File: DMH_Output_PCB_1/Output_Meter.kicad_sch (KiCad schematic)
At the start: 63 parts, among them Q1 BC558, Q2 BC558, U1 TL072, U2 LM339, U3 LM339, U4 LM339, U5 LM339, U6 LM339

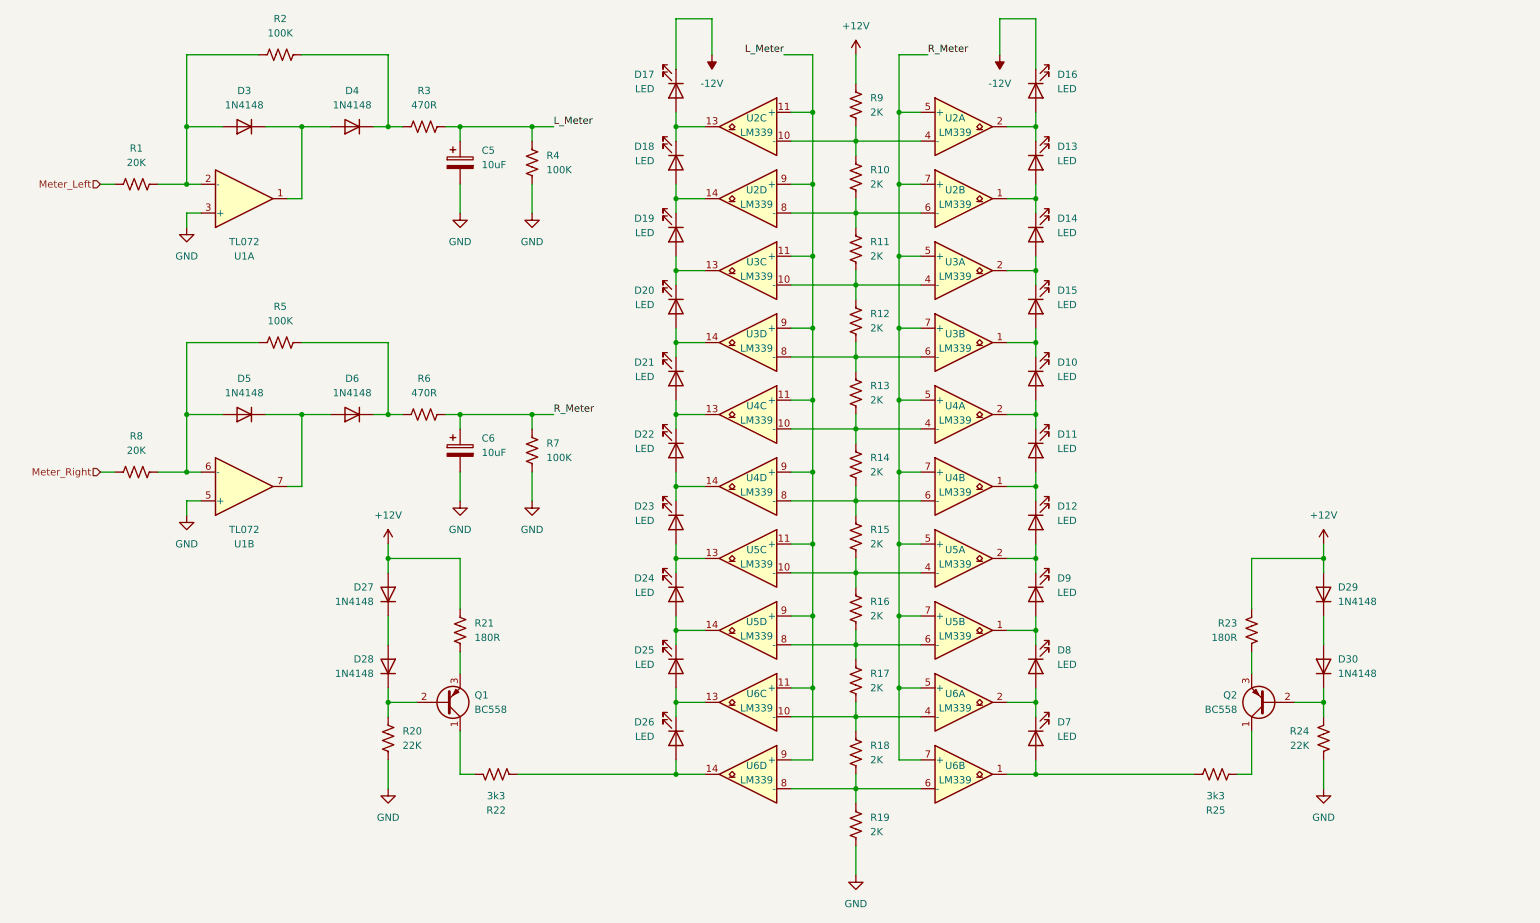
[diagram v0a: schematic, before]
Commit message: Updated output meter peak detectors
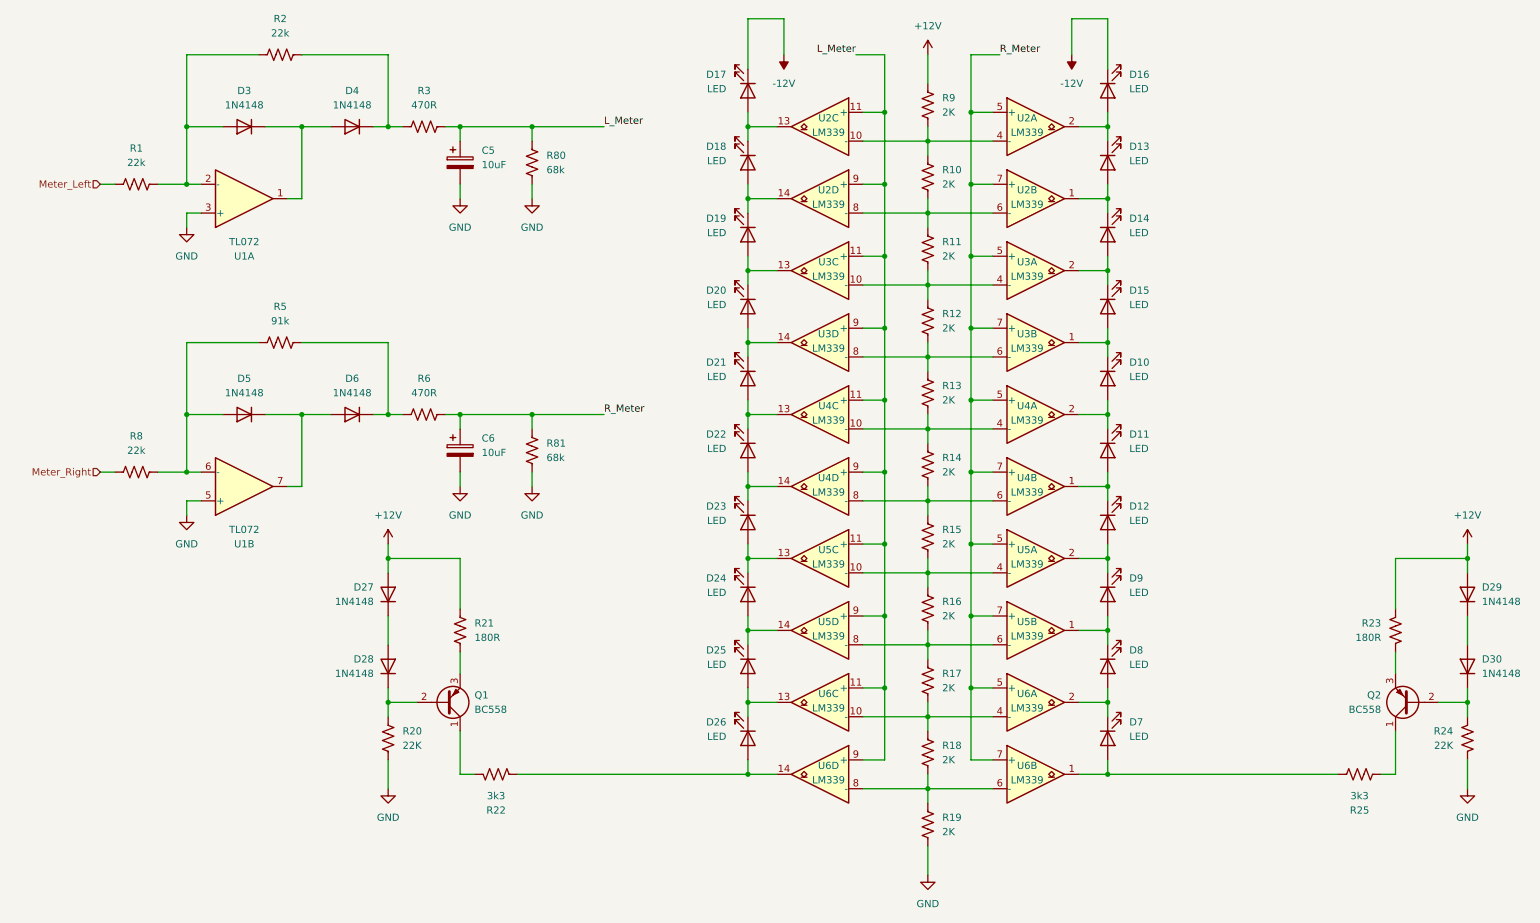
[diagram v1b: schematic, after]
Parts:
- removed R4: 100K, Resistor_THT:R_Axial_DIN0207_L6.3mm_D2.5mm_P7.62mm_Horizontal, symbol Device:R_US
- added R80: 68k, Resistor_THT:R_Axial_DIN0207_L6.3mm_D2.5mm_P7.62mm_Horizontal, symbol Device:R_US
- R1, R8: value 20K -> 22k
- R2: value 100K -> 22k
- R5: value 100K -> 91k
- R81: renamed from R7; value 100K -> 68k
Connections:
- net GND: now also R80.1
- net L_Meter: now also R80.2
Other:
- moved on the sheet: D10, D11, D12, D13, D14, D15, D16, D17, D18, D19, D20, D21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

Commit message: Updated meters resistor values
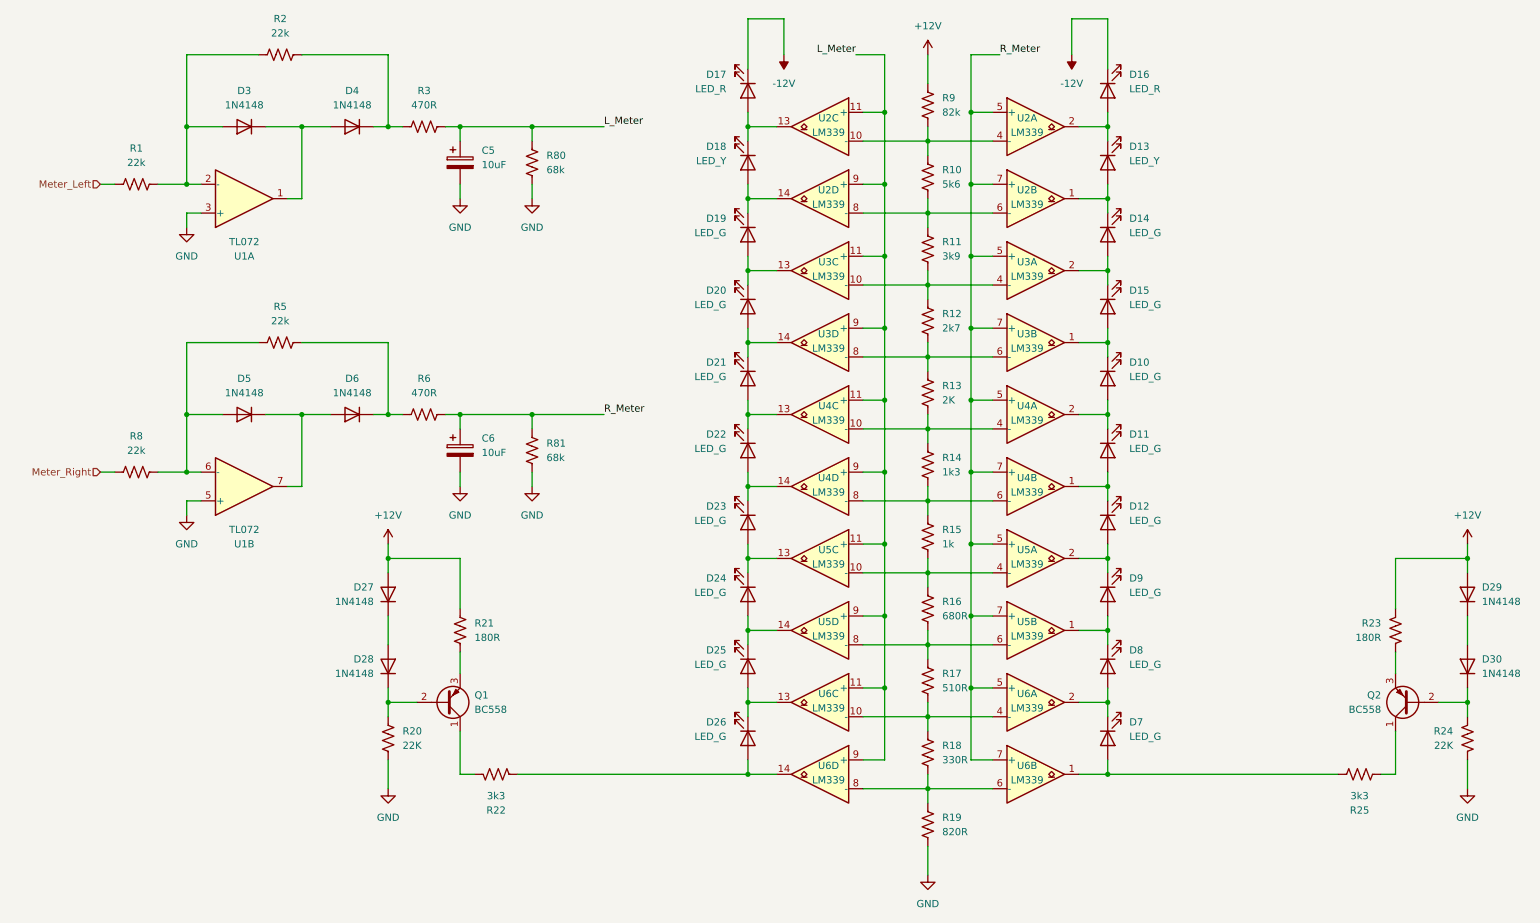
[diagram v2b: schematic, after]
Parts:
- D10, D11, D12, D14, D15, D19, D20, D21, D22, D23, D24, D25, D26, D7, D8, D9: value LED -> LED_G
- D13, D18: value LED -> LED_Y
- D16, D17: value LED -> LED_R
- R10: value 2K -> 5k6
- R11: value 2K -> 3k9
- R12: value 2K -> 2k7
- R14: value 2K -> 1k3
- R15: value 2K -> 1k
- R16: value 2K -> 680R
- R17: value 2K -> 510R
- R18: value 2K -> 330R
- R19: value 2K -> 820R
- R5: value 91k -> 22k
- R9: value 2K -> 82k
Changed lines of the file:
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@@
 			)
 		)
-		(property "Value" "LED"
+		(property "Value" "LED_G"
 			(at 207.01 145.7324 90)
 			(effects
@@
 			)
 		)
-		(property "Value" "LED"
+		(property "Value" "LED_G"
 			(at 135.89 120.3324 90)
 			(effects
@@
 			)
 		)
-		(property "Value" "91k"
+		(property "Value" "22k"
 			(at 57.15 72.39 90)
 			(effects
@@
 			)
 		)
-		(property "Value" "LED"
+		(property "Value" "LED_G"
 			(at 135.89 69.5324 90)
 			(effects
@@
 			)
 		)
-		(property "Value" "2K"
+		(property "Value" "3k9"
 			(at 173.99 60.9599 0)
 			(effects
@@
 			)
 		)
-		(property "Value" "LED"
+		(property "Value" "LED_G"
 			(at 207.01 133.0324 90)
 			(effects
@@
 			)
 		)
-		(property "Value" "LED"
+		(property "Value" "LED_G"
 			(at 207.01 69.5324 90)
 			(effects
@@
 			)
 		)
-		(property "Value" "2K"
+		(property "Value" "510R"
 			(at 173.99 137.1599 0)
 			(effects
@@
 			)
 		)
-		(property "Value" "LED"
+		(property "Value" "LED_G"
 			(at 135.89 82.2324 90)
 			(effects
@@
 			)
 		)
-		(property "Value" "LED"
+		(property "Value" "LED_Y"
 			(at 135.89 44.1324 90)
 			(effects
@@
 			)
 		)
-		(property "Value" "LED"
+		(property "Value" "LED_G"
 			(at 207.01 107.6324 90)
 			(effects
@@
 			)
 		)
-		(property "Value" "LED"
+		(property "Value" "LED_G"
 			(at 207.01 120.3324 90)
 			(effects
@@
 			)
 		)
-		(property "Value" "LED"
+		(property "Value" "LED_G"
 			(at 207.01 82.2324 90)
 			(effects
@@
 			)
 		)
-		(property "Value" "LED"
+		(property "Value" "LED_G"
 			(at 207.01 94.9324 90)
 			(effects
@@
 			)
 		)
-		(property "Value" "LED"
+		(property "Value" "LED_G"
 			(at 207.01 56.8324 90)
 			(effects
@@
 			)
 		)
-		(property "Value" "LED"
+		(property "Value" "LED_G"
 			(at 135.89 145.7324 90)
 			(effects
@@
 			)
 		)
-		(property "Value" "LED"
+		(property "Value" "LED_R"
 			(at 135.89 31.4324 90)
 			(effects
@@
 			)
 		)
-		(property "Value" "2K"
+		(property "Value" "330R"
 			(at 173.99 149.8599 0)
 			(effects
@@
 			)
 		)
-		(property "Value" "2K"
+		(property "Value" "1k"
 			(at 173.99 111.7599 0)
 			(effects
@@
 			)
 		)
-		(property "Value" "2K"
+		(property "Value" "5k6"
 			(at 173.99 48.2599 0)
 			(effects
@@
 			)
 		)
-		(property "Value" "LED"
+		(property "Value" "LED_G"
 			(at 135.89 56.8324 90)
 			(effects
@@
 			)
 		)
-		(property "Value" "LED"
+		(property "Value" "LED_Y"
 			(at 207.01 44.1324 90)
 			(effects
@@
 			)
 		)
-		(property "Value" "LED"
+		(property "Value" "LED_R"
 			(at 207.01 31.4324 90)
 			(effects
@@
 			)
 		)
-		(property "Value" "2K"
+		(property "Value" "1k3"
 			(at 173.99 99.0599 0)
 			(effects
@@
 			)
 		)
-		(property "Value" "LED"
+		(property "Value" "LED_G"
 			(at 135.89 107.6324 90)
 			(effects
@@
 			)
 		)
-		(property "Value" "2K"
+		(property "Value" "2k7"
 			(at 173.99 73.6599 0)
 			(effects
@@
 			)
 		)
-		(property "Value" "LED"
+		(property "Value" "LED_G"
 			(at 135.89 94.9324 90)
 			(effects
@@
 			)
 		)
-		(property "Value" "2K"
+		(property "Value" "82k"
 			(at 173.99 35.5599 0)
 			(effects
@@
 			)
 		)
-		(property "Value" "LED"
+		(property "Value" "LED_G"
 			(at 135.89 133.0324 90)
 			(effects
@@
 			)
 		)
-		(property "Value" "2K"
+		(property "Value" "680R"
 			(at 173.99 124.4599 0)
 			(effects
@@
 			)
 		)
-		(property "Value" "2K"
+		(property "Value" "820R"
 			(at 173.99 162.5599 0)
 			(effects

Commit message: Adjustments during breadboarding
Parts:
- R13: value 2K -> 2k
- R20, R24: value 22K -> 22k
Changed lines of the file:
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@@
 	)
 	(symbol
-		(lib_id "Amplifier_Operational:TL072")
-		(at 50.8 50.8 0)
-		(mirror x)
-		(unit 1)
-		(exclude_from_sim no)
-		(in_bom yes)
-		(on_board yes)
-		(dnp no)
-		(property "Reference" "U1"
-			(at 50.8 60.96 0)
-			(effects
-				(font
-					(size 1.27 1.27)
-				)
-			)
-		)
-		(property "Value" "TL072"
-			(at 50.8 58.42 0)
-			(effects
-				(font
-					(size 1.27 1.27)
-				)
-			)
-		)
-		(property "Footprint" "Package_DIP:DIP-8_W7.62mm_Socket"
-			(at 50.8 50.8 0)
-			(effects
-				(font
-					(size 1.27 1.27)
-				)
-				(hide yes)
-			)
-		)
-		(property "Datasheet" "http://www.ti.com/lit/ds/symlink/tl071.pdf"
-			(at 50.8 50.8 0)
-			(effects
-				(font
-					(size 1.27 1.27)
-				)
-				(hide yes)
-			)
-		)
-		(property "Description" "Dual Low-Noise JFET-Input Operational Amplifiers, DIP-8/SOIC-8"
-			(at 50.8 50.8 0)
-			(effects
-				(font
-					(size 1.27 1.27)
-				)
-				(hide yes)
-			)
-		)
-		(property "Function" ""
-			(at 50.8 50.8 0)
-			(effects
-				(font
-					(size 1.27 1.27)
-				)
-			)
-		)
-		(pin "5"
-		)
-		(pin "2"
-		)
-		(pin "4"
-		)
-		(pin "3"
-		)
-		(pin "1"
-		)
-		(pin "6"
-		)
-		(pin "7"
-		)
-		(pin "8"
-		)
-		(instances
-			(project "DMH_Output_PCB_1"
-				(path "/58f4306d-5387-4983-bb08-41a2313fd315/91d96a83-7777-458d-a0c8-9961efcb16a5"
-					(reference "U1")
-					(unit 1)
-				)
-			)
-		)
-	)
-	(symbol
 		(lib_id "power:GND")
 		(at 76.2 154.94 0)
@@
 	)
 	(symbol
-		(lib_id "Amplifier_Operational:TL072")
-		(at 50.8 101.6 0)
-		(mirror x)
-		(unit 2)
+		(lib_id "Device:R_US")
+		(at 101.6 95.25 180)
+		(unit 1)
 		(exclude_from_sim no)
 		(in_bom yes)
 		(on_board yes)
 		(dnp no)
-		(property "Reference" "U1"
-			(at 50.8 111.76 0)
+		(fields_autoplaced yes)
+		(property "Reference" "R81"
+			(at 104.14 93.9799 0)
 			(effects
 				(font
 					(size 1.27 1.27)
 				)
+				(justify right)
 			)
 		)
-		(property "Value" "TL072"
-			(at 50.8 109.22 0)
+		(property "Value" "68k"
+			(at 104.14 96.5199 0)
 			(effects
 				(font
 					(size 1.27 1.27)
 				)
+				(justify right)
 			)
 		)
-		(property "Footprint" "Package_DIP:DIP-8_W7.62mm_Socket"
-			(at 50.8 101.6 0)
+		(property "Footprint" "Resistor_THT:R_Axial_DIN0207_L6.3mm_D2.5mm_P7.62mm_Horizontal"
+			(at 100.584 94.996 90)
 			(effects
 				(font
@@
 			)
 		)
-		(property "Datasheet" "http://www.ti.com/lit/ds/symlink/tl071.pdf"
-			(at 50.8 101.6 0)
+		(property "Datasheet" "~"
+			(at 101.6 95.25 0)
 			(effects
 				(font
@@
 			)
 		)
-		(property "Description" "Dual Low-Noise JFET-Input Operational Amplifiers, DIP-8/SOIC-8"
-			(at 50.8 101.6 0)
+		(property "Description" "Resistor, US symbol"
+			(at 101.6 95.25 0)
 			(effects
 				(font
@@
 			)
 		)
-		(property "Function" ""
-			(at 50.8 101.6 0)
-			(effects
-				(font
-					(size 1.27 1.27)
-				)
-			)
-		)
-		(pin "5"
-		)
 		(pin "2"
 		)
-		(pin "4"
-		)
-		(pin "3"
-		)
 		(pin "1"
 		)
-		(pin "6"
-		)
-		(pin "7"
-		)
-		(pin "8"
-		)
 		(instances
 			(project "DMH_Output_PCB_1"
 				(path "/58f4306d-5387-4983-bb08-41a2313fd315/91d96a83-7777-458d-a0c8-9961efcb16a5"
-					(reference "U1")
-					(unit 2)
+					(reference "R81")
+					(unit 1)
 				)
 			)
@@
 	)
 	(symbol
-		(lib_id "Device:R_US")
-		(at 101.6 95.25 180)
+		(lib_id "Amplifier_Operational:TL072")
+		(at 50.8 50.8 0)
+		(mirror x)
 		(unit 1)
 		(exclude_from_sim no)
@@
 		(on_board yes)
 		(dnp no)
-		(fields_autoplaced yes)
-		(property "Reference" "R81"
-			(at 104.14 93.9799 0)
+		(property "Reference" "U1"
+			(at 50.8 60.96 0)
 			(effects
 				(font
 					(size 1.27 1.27)
 				)
-				(justify right)
 			)
 		)
-		(property "Value" "68k"
-			(at 104.14 96.5199 0)
+		(property "Value" "TL072"
+			(at 50.8 58.42 0)
 			(effects
 				(font
 					(size 1.27 1.27)
 				)
-				(justify right)
 			)
 		)
-		(property "Footprint" "Resistor_THT:R_Axial_DIN0207_L6.3mm_D2.5mm_P7.62mm_Horizontal"
-			(at 100.584 94.996 90)
+		(property "Footprint" "Package_DIP:DIP-8_W7.62mm_Socket"
+			(at 50.8 50.8 0)
 			(effects
 				(font
@@
 			)
 		)
-		(property "Datasheet" "~"
-			(at 101.6 95.25 0)
+		(property "Datasheet" "http://www.ti.com/lit/ds/symlink/tl071.pdf"
+			(at 50.8 50.8 0)
 			(effects
 				(font
@@
 			)
 		)
-		(property "Description" "Resistor, US symbol"
-			(at 101.6 95.25 0)
+		(property "Description" "Dual Low-Noise JFET-Input Operational Amplifiers, DIP-8/SOIC-8"
+			(at 50.8 50.8 0)
 			(effects
 				(font
@@
 			)
 		)
+		(pin "7"
+		)
 		(pin "2"
 		)
+		(pin "6"
+		)
+		(pin "3"
+		)
+		(pin "8"
+		)
+		(pin "4"
+		)
 		(pin "1"
 		)
+		(pin "5"
+		)
 		(instances
-			(project "DMH_Output_PCB_1"
+			(project ""
 				(path "/58f4306d-5387-4983-bb08-41a2313fd315/91d96a83-7777-458d-a0c8-9961efcb16a5"
-					(reference "R81")
+					(reference "U1")
 					(unit 1)
 				)
@@
 			)
 		)
-		(property "Value" "22K"
+		(property "Value" "22k"
 			(at 264.16 147.3199 0)
 			(effects
@@
 			)
 		)
-		(property "Value" "22K"
+		(property "Value" "22k"
 			(at 78.74 147.3199 0)
 			(effects
@@
 			)
 		)
-		(property "Value" "2K"
+		(property "Value" "2k"
 			(at 173.99 86.3599 0)
 			(effects
@@
 				)
 			)
+		)
+	)
+	(symbol
+		(lib_id "Amplifier_Operational:TL072")
+		(at 50.8 101.6 0)
+		(mirror x)
+		(unit 2)
+		(exclude_from_sim no)
+		(in_bom yes)
+		(on_board yes)
+		(dnp no)
+		(property "Reference" "U1"
+			(at 50.8 111.76 0)
+			(effects
+				(font
+					(size 1.27 1.27)
+				)
+			)
+		)
+		(property "Value" "TL072"
+			(at 50.8 109.22 0)
+			(effects
+				(font
+					(size 1.27 1.27)
+				)
+			)
+		)
+		(property "Footprint" "Package_DIP:DIP-8_W7.62mm_Socket"
+			(at 50.8 101.6 0)
+			(effects
+				(font
+					(size 1.27 1.27)
+				)
+				(hide yes)
+			)
+		)
+		(property "Datasheet" "http://www.ti.com/lit/ds/symlink/tl071.pdf"
+			(at 50.8 101.6 0)
+			(effects
+				(font
+					(size 1.27 1.27)
+				)
+				(hide yes)
+			)
+		)
+		(property "Description" "Dual Low-Noise JFET-Input Operational Amplifiers, DIP-8/SOIC-8"
+			(at 50.8 101.6 0)
+			(effects
+				(font
+					(size 1.27 1.27)
+				)
+				(hide yes)
+			)
+		)
+		(pin "7"
+		)
+		(pin "2"
+		)
+		(pin "6"
+		)
+		(pin "3"
+		)
+		(pin "8"
+		)
+		(pin "4"
+		)
+		(pin "1"
+		)
+		(pin "5"
+		)
+		(instances
+			(project ""
+				(path "/58f4306d-5387-4983-bb08-41a2313fd315/91d96a83-7777-458d-a0c8-9961efcb16a5"
+					(reference "U1")
+					(unit 2)
+				)
+			)

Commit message: Adjustments during breadboarding
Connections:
- net L_Meter: now also U2.5 (+), U2.7 (+), U3.5 (+), U3.7 (+), U4.5 (+), U4.7 (+), U5.5 (+), U5.7 (+), U6.5 (+), U6.7 (+); no longer U2.11 (+), U2.9 (+), U3.11 (+), U3.9 (+), U4.11 (+), U4.9 (+), U5.11 (+), U5.9 (+), U6.11 (+), U6.9 (+)
- net R_Meter: now also U2.11 (+), U2.9 (+), U3.11 (+), U3.9 (+), U4.11 (+), U4.9 (+), U5.11 (+), U5.9 (+), U6.11 (+), U6.9 (+); no longer U2.5 (+), U2.7 (+), U3.5 (+), U3.7 (+), U4.5 (+), U4.7 (+), U5.5 (+), U5.7 (+), U6.5 (+), U6.7 (+)
- net at D8.1 (K), D9.2 (A): now also U5.13; no longer U5.1
- net at U5.6 (-), U5.8 (-): now also R15.1, R16.2; no longer R16.1, R17.2
- net at D11.2 (A), D12.1 (K): now also U4.13; no longer U4.1
- net at U4.6 (-), U4.8 (-): now also R13.1, R14.2; no longer R14.1, R15.2
- net at U3.10 (-), U3.4 (-): now also R12.1, R13.2; no longer R11.1, R12.2
- net at D19.2 (A), D20.1 (K): now also U3.1; no longer U3.13
- net at D7.1 (K), D8.2 (A): now also U6.14; no longer U6.2
- net at D7.2 (A), R25.2: now also U6.13; no longer U6.1
- net at D23.2 (A), D24.1 (K): now also U5.1; no longer U5.13
- net at D24.2 (A), D25.1 (K): now also U5.2; no longer U5.14
- net at D20.2 (A), D21.1 (K): now also U3.2; no longer U3.14
- net at R10.1, R11.2: now also U2.10 (-), U2.4 (-); no longer U2.6 (-), U2.8 (-)
- net at D10.2 (A), D11.1 (K): now also U4.14; no longer U4.2
- net at U4.10 (-), U4.4 (-): now also R14.1, R15.2; no longer R13.1, R14.2
- net at D14.2 (A), D15.1 (K): now also U3.14; no longer U3.2
- net at D10.1 (K), D15.2 (A): now also U3.13; no longer U3.1
- net at D22.2 (A), D23.1 (K): now also U4.2; no longer U4.14
- net at D26.2 (A), R22.2: now also U6.2; no longer U6.14
- net at D18.2 (A), D19.1 (K): now also U2.2; no longer U2.14
- net at R17.1, R18.2: now also U6.6 (-), U6.8 (-); no longer U6.10 (-), U6.4 (-)
- net at D21.2 (A), D22.1 (K): now also U4.1; no longer U4.13
- net at R18.1, R19.2: now also U6.10 (-), U6.4 (-); no longer U6.6 (-), U6.8 (-)
- net at D25.2 (A), D26.1 (K): now also U6.1; no longer U6.13
- net at D17.2 (A), D18.1 (K): now also U2.1; no longer U2.13
- net at U3.6 (-), U3.8 (-): now also R11.1, R12.2; no longer R12.1, R13.2
- net at D12.2 (A), D9.1 (K): now also U5.14; no longer U5.2
- net at D13.1 (K), D16.2 (A): now also U2.14; no longer U2.2
- net at R10.2, R9.1: now also U2.6 (-), U2.8 (-); no longer U2.10 (-), U2.4 (-)
- net at D13.2 (A), D14.1 (K): now also U2.13; no longer U2.1
- net at U5.10 (-), U5.4 (-): now also R16.1, R17.2; no longer R15.1, R16.2
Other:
- moved on the sheet: U2A, U2B, U2C, U2D, U3A, U3B, U3C, U3D, U4A, U4B, U4C, U4D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
